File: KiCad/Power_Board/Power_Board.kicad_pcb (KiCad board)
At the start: 4 copper layers, 101.6 x 63.5 mm, 143 parts, among them P1 CONN_LEFT_TOP, P10 CONN_02X01, P2 CONN_RIGHT_TOP, P3 CONN_LEFT_BOTTOM, P4 CONN_RIGHT_BOTTOM, P5 CONN_02X01, P6 CONN_02X01, P7 CONN_02X01, P8 CONN_02X01, P9 CONN_02X01, Q1 IRLL024NQ, U1 AD1583, U10 ADP7142_CSP, U11 ADP7182_CSP, U12 ADP3335_CSP, U2 MAX5259, U3 MAX5259, U4 TPS63030, U5 TPS63030, U6 TPS63030, U7 MAX152x, U8 ADP5070, U9 TPS63030

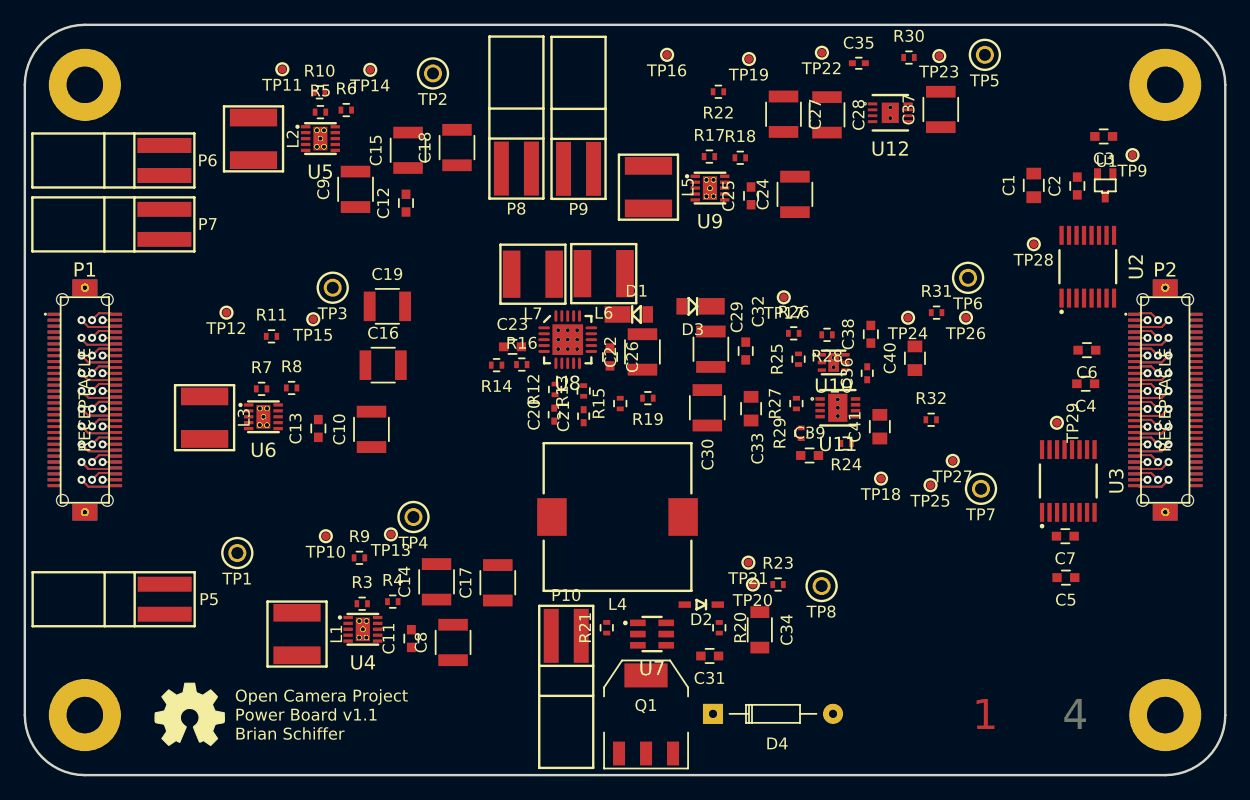
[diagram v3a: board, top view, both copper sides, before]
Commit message: Some layout progress.
Properly placed and oriented parts for compact layout of individual
modules.
Added zones of copper around the converters as appropriate.
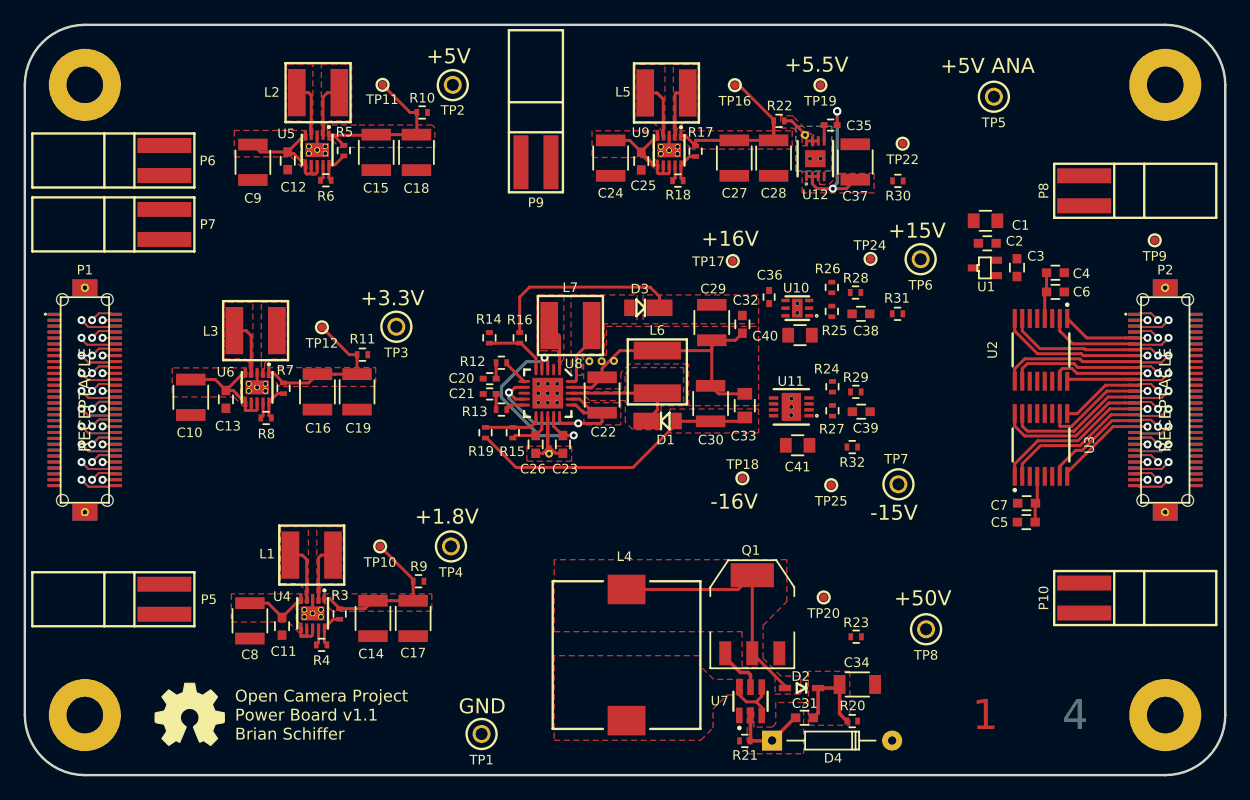
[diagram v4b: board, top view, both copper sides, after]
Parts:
- removed TP13, TP14, TP15, TP21, TP23, TP26, TP27, TP28, TP29: Test_Point, OpenCamera:TEST_POINT_SMD
- added ?: , OpenCamera:STITCH_VIA, F.Cu at (136.7, 104.7)
- added ?: , OpenCamera:STITCH_VIA, F.Cu at (137.7, 104.7)
- added ?: , OpenCamera:STITCH_VIA, F.Cu at (138.8, 104.6)
- added ?: , OpenCamera:STITCH_VIA, F.Cu at (133.3, 112.5)
- added ?: , OpenCamera:STITCH_VIA, F.Cu at (154.9, 85.5)
- D4: footprint Diodes_ThroughHole:Diode_DO-35_SOD27_Horizontal_RM10 -> OpenCamera:Diode_DO-35
- moved P8 48.1 mm to (178.6, 90.2), turned to 270 degrees
- moved P10 44.0 mm to (178.6, 124.7), turned to 270 degrees
- moved TP1 25.7 mm to (127.6, 136.2)
- moved C8 17.3 mm to (108.0, 126.6), turned to 270 degrees
- moved C24 15.9 mm to (138.5, 87.5), turned to 270 degrees
- moved C10 15.5 mm to (102.9, 107.7), turned to 270 degrees
- moved R21 15.1 mm to (149.8, 136.8), turned to 180 degrees
- moved R19 14.0 mm to (127.9, 110.7), turned to 90 degrees
- moved R20 13.7 mm to (158.9, 135.1), turned to 0 degrees
- moved C3 13.3 mm to (172.9, 96.7), turned to 90 degrees
- moved Q1 12.4 mm to (150.5, 126.1)
- moved U1 12.4 mm to (170.2, 96.8), turned to 270 degrees
- moved TP18 11.7 mm to (149.6, 114.6)
- moved L4 11.7 mm to (139.8, 129.5), turned to 90 degrees
- moved D2 11.0 mm to (154.6, 132.3)
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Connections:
- net GNDA renamed GND
- U2 pad 1: /connectors/R6 -> /connectors/R5
- U2 pad 10: /connectors/R12 -> /connectors/R10
- U2 pad 15: /connectors/R8 -> /connectors/R11
- U2 pad 16: /connectors/R7 -> /connectors/R12
- U2 pad 2: /connectors/R5 -> /connectors/R6
- U2 pad 7: /connectors/R9 -> /connectors/R7
- U2 pad 8: /connectors/R10 -> /connectors/R8
- U2 pad 9: /connectors/R11 -> /connectors/R9
- U3 pad 1: /connectors/R14 -> /connectors/R17
- U3 pad 10: /connectors/R20 -> /connectors/R14
- U3 pad 15: /connectors/R16 -> /connectors/R15
- U3 pad 16: /connectors/R15 -> /connectors/R16
- U3 pad 2: /connectors/R13 -> /connectors/R18
- U3 pad 7: /connectors/R17 -> /connectors/R19
- U3 pad 8: /connectors/R18 -> /connectors/R20
- U3 pad 9: /connectors/R19 -> /connectors/R13
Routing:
- net GND: track 0.00 -> 42.9 mm
- net /Analog_Power/-16V: track 0.00 -> 24.9 mm
- net Net-(D2-Pad1): track 0.00 -> 21.8 mm
- net Net-(C22-Pad1): track 0.00 -> 21.0 mm, vias 0 -> 2
- net Net-(C23-Pad2): track 0.00 -> 18.1 mm, vias 0 -> 2
- net /Analog_Power/+16V: track 0.00 -> 16.5 mm
- net Net-(C27-Pad1): track 0.00 -> 14.9 mm
- net Net-(C15-Pad1): track 0.00 -> 14.8 mm
- net Net-(C14-Pad1): track 0.00 -> 13.9 mm
- net Net-(C16-Pad1): track 0.00 -> 13.7 mm
- net Net-(C35-Pad1): track 0.00 -> 13.6 mm, vias 0 -> 3
- net /connectors/R17: track 2.24 -> 15.3 mm
- net /connectors/R16: track 4.55 -> 17.2 mm
- net /connectors/R18: track 6.35 -> 18.6 mm
- net /connectors/R8: track 2.24 -> 14.2 mm
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- added copper zone on F.Cu, net /Analog_Power/+16V
- added copper zone on F.Cu, net /Analog_Power/-16V
- added copper zone on B.Cu, net /Analog_Power/5.5V
- added copper zone on F.Cu, net /Analog_Power/5.5V
- added copper zone on F.Cu, net GND
- added copper zone on F.Cu, net Net-(C10-Pad1)
- added copper zone on F.Cu, net Net-(C11-Pad1)
- added copper zone on F.Cu, net Net-(C12-Pad1)
- added copper zone on F.Cu, net Net-(C14-Pad1)
- added copper zone on F.Cu, net Net-(C15-Pad1)
- added copper zone on F.Cu, net Net-(C16-Pad1)
- added copper zone on F.Cu, net Net-(C22-Pad1)
- added copper zone on F.Cu, net Net-(C24-Pad1)
- added copper zone on F.Cu, net Net-(C27-Pad1)
- added copper zone on F.Cu, net Net-(C31-Pad1)
- added copper zone on F.Cu, net Net-(C31-Pad2)
- added copper zone on F.Cu, net Net-(C35-Pad1)
- added copper zone on F.Cu, net Net-(D1-Pad2)
- added copper zone on F.Cu, net Net-(D2-Pad1)
- added copper zone on F.Cu, net Net-(D3-Pad1)
- added copper zone on F.Cu, net Net-(L1-Pad1)
- added copper zone on F.Cu, net Net-(L1-Pad2)
- added copper zone on F.Cu, net Net-(L2-Pad1)
- added copper zone on F.Cu, net Net-(L2-Pad2)
- added copper zone on F.Cu, net Net-(L3-Pad1)
- added copper zone on F.Cu, net Net-(L3-Pad2)
- added copper zone on F.Cu, net Net-(L4-Pad1)
- added copper zone on F.Cu, net Net-(L5-Pad1)
- added copper zone on F.Cu, net Net-(L5-Pad2)
- added copper zone on F.Cu, net Net-(L7-Pad1)
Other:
- board text added: "+1.8V"
- board text added: "+15V"
- board text added: "+16V"
- board text added: "+3.3V"
- board text added: "+5.5V"
- board text added: "+50V"
- board text added: "+5V"
- board text added: "+5V ANA"
- board text added: "-15V"
- board text added: "-16V"
- board text added: "GND"

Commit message: All nets routed! No DRC errors.
Still needs some cleanup:
-Check ground plane continuity.
-Thicken power traces where possible.
-Move SPI lines out of the way.
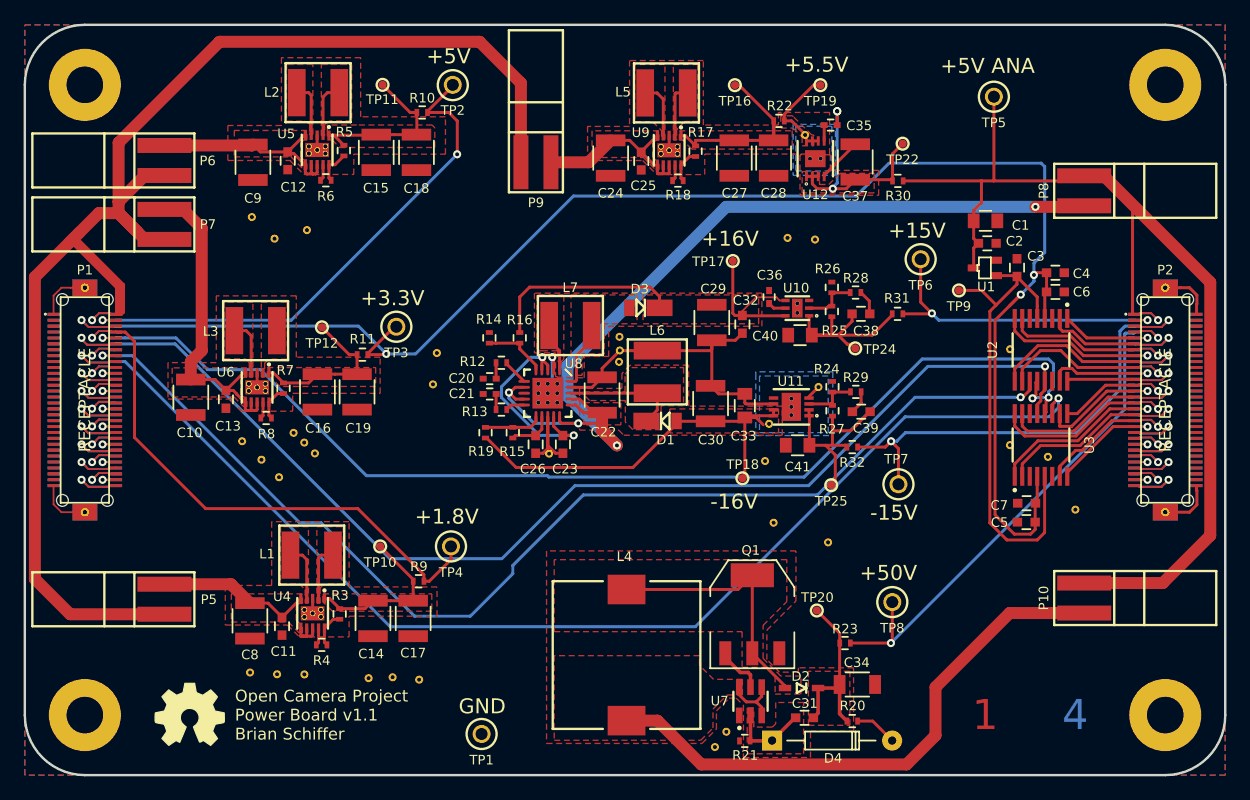
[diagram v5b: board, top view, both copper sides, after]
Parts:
- added ?: , OpenCamera:STITCH_VIA, F.Cu at (113.4, 112.5)
- added ?: , OpenCamera:STITCH_VIA, F.Cu at (155.8, 94.4)
- added ?: , OpenCamera:STITCH_VIA, F.Cu at (153.5, 94.2)
- added ?: , OpenCamera:STITCH_VIA, F.Cu at (151.5, 113.1)
- added ?: , OpenCamera:STITCH_VIA, F.Cu at (156.9, 120.0)
- added ?: , OpenCamera:STITCH_VIA, F.Cu at (152.3, 118.3)
- added ?: , OpenCamera:STITCH_VIA, F.Cu at (107.3, 111.4)
- added ?: , OpenCamera:STITCH_VIA, F.Cu at (123.4, 106.6)
- added ?: , OpenCamera:STITCH_VIA, F.Cu at (123.8, 104.0)
- added ?: , OpenCamera:STITCH_VIA, F.Cu at (110.0, 94.3)
- added ?: , OpenCamera:STITCH_VIA, F.Cu at (112.8, 93.6)
- added ?: , OpenCamera:STITCH_VIA, F.Cu at (112.5, 111.6)
- added ?: , OpenCamera:STITCH_VIA, F.Cu at (108.1, 92.5)
- added ?: , OpenCamera:STITCH_VIA, F.Cu at (108.9, 113.0)
- added ?: , OpenCamera:STITCH_VIA, F.Cu at (110.4, 114.5)
- added ?: , OpenCamera:STITCH_VIA, F.Cu at (122.3, 131.6)
- added ?: , OpenCamera:STITCH_VIA, F.Cu at (120.0, 131.4)
- added ?: , OpenCamera:STITCH_VIA, F.Cu at (112.6, 131.2)
- added ?: , OpenCamera:STITCH_VIA, F.Cu at (110.2, 131.2)
- added ?: , OpenCamera:STITCH_VIA, F.Cu at (108.0, 131.0)
- added ?: , OpenCamera:STITCH_VIA, F.Cu at (118.0, 131.5)
- added ?: , OpenCamera:STITCH_VIA, F.Cu at (111.6, 110.7)
- added ?: , OpenCamera:STITCH_VIA, F.Cu at (172.3, 103.7)
- added ?: , OpenCamera:STITCH_VIA, F.Cu at (151.9, 110.0)
- added ?: , OpenCamera:STITCH_VIA, F.Cu at (156.1, 106.9)
- added ?: , OpenCamera:STITCH_VIA, F.Cu at (172.3, 111.8)
- added ?: , OpenCamera:STITCH_VIA, F.Cu at (175.5, 112.8)
- added ?: , OpenCamera:STITCH_VIA, F.Cu at (177.8, 117.2)
- added ?: , OpenCamera:STITCH_VIA, F.Cu at (148.3, 136.0)
- added ?: , OpenCamera:STITCH_VIA, F.Cu at (147.3, 137.3)
- moved TP9 17.1 mm to (168.0, 98.7)
- moved TP24 7.68 mm to (159.2, 103.6)
- moved TP8 3.67 mm to (162.3, 125.1)
- moved ? 3.29 mm to (139.2, 102.6)
- moved ? 1.79 mm to (139.3, 103.8)
- moved TP20 1.25 mm to (155.9, 125.8)
- moved R23 1.08 mm to (158.3, 128.5)
- moved ? 0.44 mm to (139.2, 104.7)
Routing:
- net /connectors/L1: track 4.56 -> 148.5 mm
- net /Digital_Power/3.3V: track 14.3 -> 144.4 mm, vias 1 -> 4
- net /connectors/L9: track 6.33 -> 105.4 mm, vias 1 -> 2
- net /connectors/L6: track 6.48 -> 103.7 mm, vias 1 -> 2
- net /connectors/L5: track 2.28 -> 98.4 mm, vias 1 -> 3
- net /connectors/L8: track 2.24 -> 97.9 mm, vias 1 -> 2
- net /Analog_Power/5Va: track 4.56 -> 96.1 mm
- net Net-(C22-Pad1): track 21.0 -> 82.2 mm, vias 2 -> 4
- net Net-(L4-Pad1): track 5.12 -> 53.1 mm
- net /Digital_Power/1.8V: track 4.57 -> 48.6 mm
- net /Digital_Power/5V: track 2.25 -> 45.9 mm, vias 1 -> 2
- net /Analog_Power/50Va: track 4.57 -> 46.8 mm, vias 1 -> 2
- net /Vref_3V: track 0.00 -> 41.8 mm
- net /Analog_Power/-15Va: track 6.33 -> 40.8 mm, vias 1 -> 2
- net GND: track 42.9 -> 74.1 mm, vias 0 -> 1
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- added copper zone on B.Cu, net /Analog_Power/-16V
- added copper zone on B.Cu, net GND

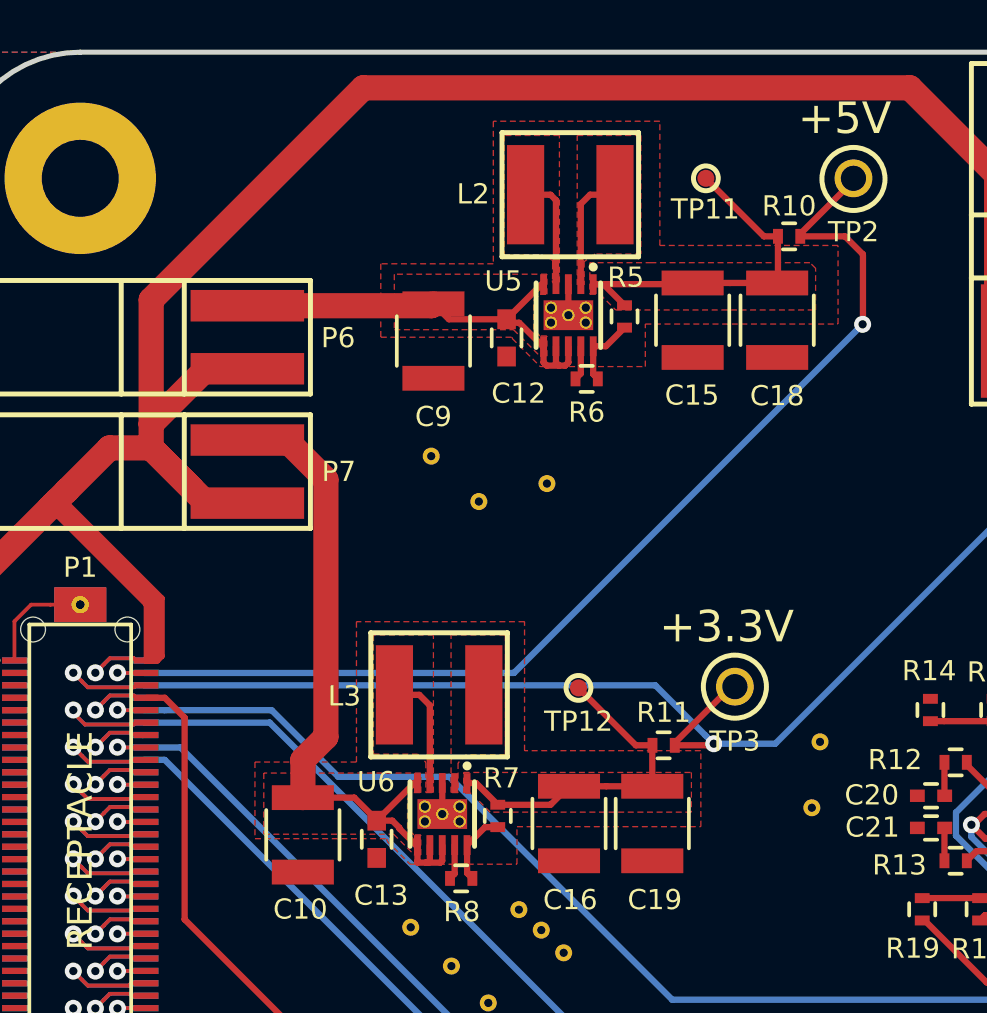
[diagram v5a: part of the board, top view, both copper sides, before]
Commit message: Added a Vin test clip.
Also did a bit of copper pour cutout cleanup.
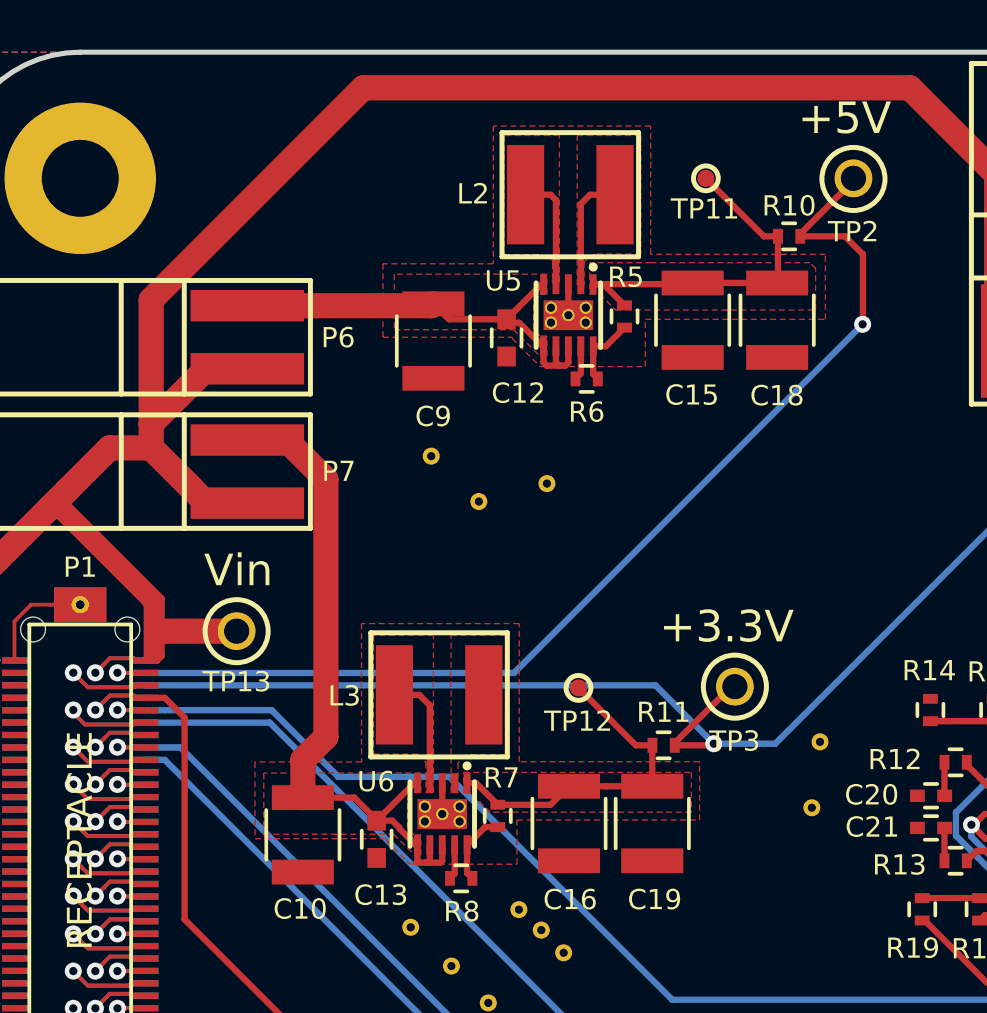
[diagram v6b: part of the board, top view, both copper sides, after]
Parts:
- added TP13: Test_Point, OpenCamera:TEST_CLIP, F.Cu at (100.3, 99.5)
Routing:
- net /connectors/L1: track 148.5 -> 151.5 mm
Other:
- board text added: "Vin"
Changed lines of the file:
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@@
 (kicad_pcb (version 4) (host pcbnew "(2015-04-19 BZR 5613)-product")
   (general
-    (links 542)
+    (links 543)
     (no_connects 0)
-    (area 83.190267 68.4732 202.615715 140.85886)
+    (area 88.798399 76.098399 190.601601 139.801601)
     (thickness 1.6)
-    (drawings 26)
-    (tracks 1374)
+    (drawings 27)
+    (tracks 1377)
     (zones 0)
-    (modules 169)
+    (modules 170)
     (nets 116)
   )
@@
     (35 F.Paste user hide)
     (36 B.SilkS user)
-    (37 F.SilkS user hide)
+    (37 F.SilkS user)
     (38 B.Mask user)
     (39 F.Mask user)
@@
   )
   (setup
-    (last_trace_width 0.1524)
+    (last_trace_width 1.016)
     (user_trace_width 0.1524)
     (user_trace_width 0.2032)
@@
       (net 71 /Analog_Power/-16V))
   )
+  (module OpenCamera:TEST_CLIP (layer F.Cu)
+    (at 100.2792 99.5172)
+    (fp_text reference TP13 (at 0.0127 2.0447) (layer F.SilkS)
+      (effects (font (size 0.8128 0.8128) (thickness 0.127)))
+    )
+    (fp_text value Test_Point (at 0 -2.13) (layer F.Fab)
+      (effects (font (size 1 1) (thickness 0.15)))
+    )
+    (fp_circle (center 0 0) (end 1.27 0.02) (layer F.SilkS) (width 0.2))
+    (pad 1 thru_hole circle (at 0 0) (size 1.524 1.524) (drill 1.016) (layers *.Cu *.Mask F.SilkS)
+      (net 1 /connectors/L1))
+  )
+  (gr_text Vin (at 100.3554 97.0788) (layer F.SilkS)
+    (effects (font (thickness 0.2032)))
+  )
   (gr_text +50V (at 161.9885 122.5931) (layer F.SilkS)
     (effects (font (thickness 0.2032)))
@@
   (gr_arc (start 93.98 81.28) (end 88.9 81.28) (angle 90) (layer Edge.Cuts) (width 0.2032))
   (gr_arc (start 185.42 134.62) (end 190.5 134.62) (angle 90) (layer Edge.Cuts) (width 0.2032))
+  (segment (start 97.2566 100.5205) (end 97.2566 99.54006) (width 0.254) (layer F.Cu) (net 1))
+  (segment (start 97.2566 99.54006) (end 97.2566 98.1964) (width 0.254) (layer F.Cu) (net 1))
+  (segment (start 100.2792 99.5172) (end 97.27946 99.5172) (width 1.016) (layer F.Cu) (net 1))
+  (segment (start 97.27946 99.5172) (end 97.2566 99.54006) (width 1.016) (layer F.Cu) (net 1))
   (via (at 94.5896 101.1936) (size 0.6858) (drill 0.3302) (layers F.Cu B.Cu) (net 1))
   (segment (start 96.63 100.7) (end 96.6156 100.6856) (width 0.1524) (layer F.Cu) (net 1))
@@
   (segment (start 96.8739 100.7) (end 97.07073 100.50317) (width 0.254) (layer F.Cu) (net 1))
   (segment (start 97.07073 98.31648) (end 93.232183 94.477933) (width 0.254) (layer F.Cu) (net 1))
-  (segment (start 97.2566 100.5205) (end 97.2566 98.1964) (width 0.254) (layer F.Cu) (net 1))
   (segment (start 97.0771 100.7) (end 97.2566 100.5205) (width 0.254) (layer F.Cu) (net 1))
   (segment (start 96.63 100.7) (end 97.0771 100.7) (width 0.254) (layer F.Cu) (net 1))
@@
     )
     (polygon
-      (pts        (xy 118.9736 107.3912) (xy 118.9736 104.3305) (xy 111.8743 104.3305) (xy 111.8743 99.1362) (xy 105.1052 99.1362)
-        (xy 105.1052 104.7877) (xy 101.0158 104.7877) (xy 101.0158 107.8738) (xy 106.3371 107.8738) (xy 106.3371 107.9754)
-        (xy 107.2642 108.9025) (xy 111.5695 108.9025) (xy 111.5695 107.3912)
+      (pts        (xy 118.9228 107.1245) (xy 118.9228 104.775) (xy 111.6584 104.775) (xy 111.6584 99.2124) (xy 105.3084 99.2124)
+        (xy 105.3084 104.7877) (xy 101.0158 104.7877) (xy 101.0158 107.8738) (xy 106.3371 107.8738) (xy 106.3371 107.9754)
+        (xy 107.2642 108.9025) (xy 111.5695 108.9025) (xy 111.5695 107.1245)
       )
     )
     (polygon
-      (pts        (xy 124.4981 87.1474) (xy 124.4981 83.9851) (xy 117.3226 83.9851) (xy 117.3226 78.9813) (xy 110.617 78.9813)
-        (xy 110.617 84.7217) (xy 106.0831 84.7217) (xy 106.0831 87.6808) (xy 111.379 87.6808) (xy 111.379 87.7316)
-        (xy 112.5093 88.8619) (xy 116.7384 88.8619) (xy 116.7384 87.1474)
+      (pts        (xy 123.9901 86.9569) (xy 123.9901 84.3407) (xy 116.9543 84.3407) (xy 116.9543 79.1718) (xy 110.617 79.1718)
+        (xy 110.617 84.7217) (xy 106.172 84.7217) (xy 106.172 87.6808) (xy 111.379 87.6808) (xy 111.379 87.7316)
+        (xy 112.5093 88.8619) (xy 116.7384 88.8619) (xy 116.7384 86.9569)
       )
     )
